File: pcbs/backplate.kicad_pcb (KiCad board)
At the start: 2 copper layers, 130.3 x 107.9 mm, 5 parts

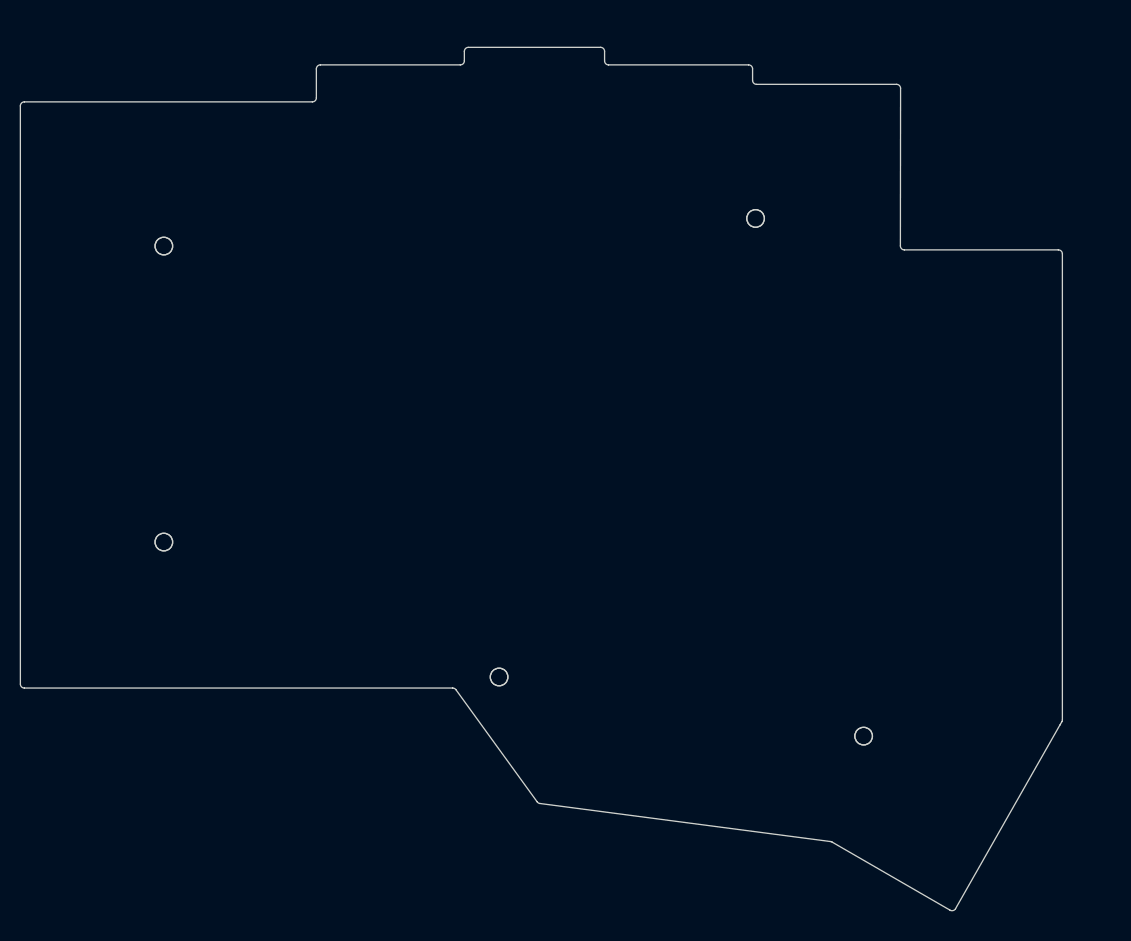
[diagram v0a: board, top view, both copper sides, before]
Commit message: fix(pcb): increase key spacing and correct power switch
Set the PG1316S key pitch to 19.5 mm in both axes and regenerate the tracked PCB and outline artifacts.

Keep the power switch mapping consistent with the intended on/off orientation while preserving the original board outline.
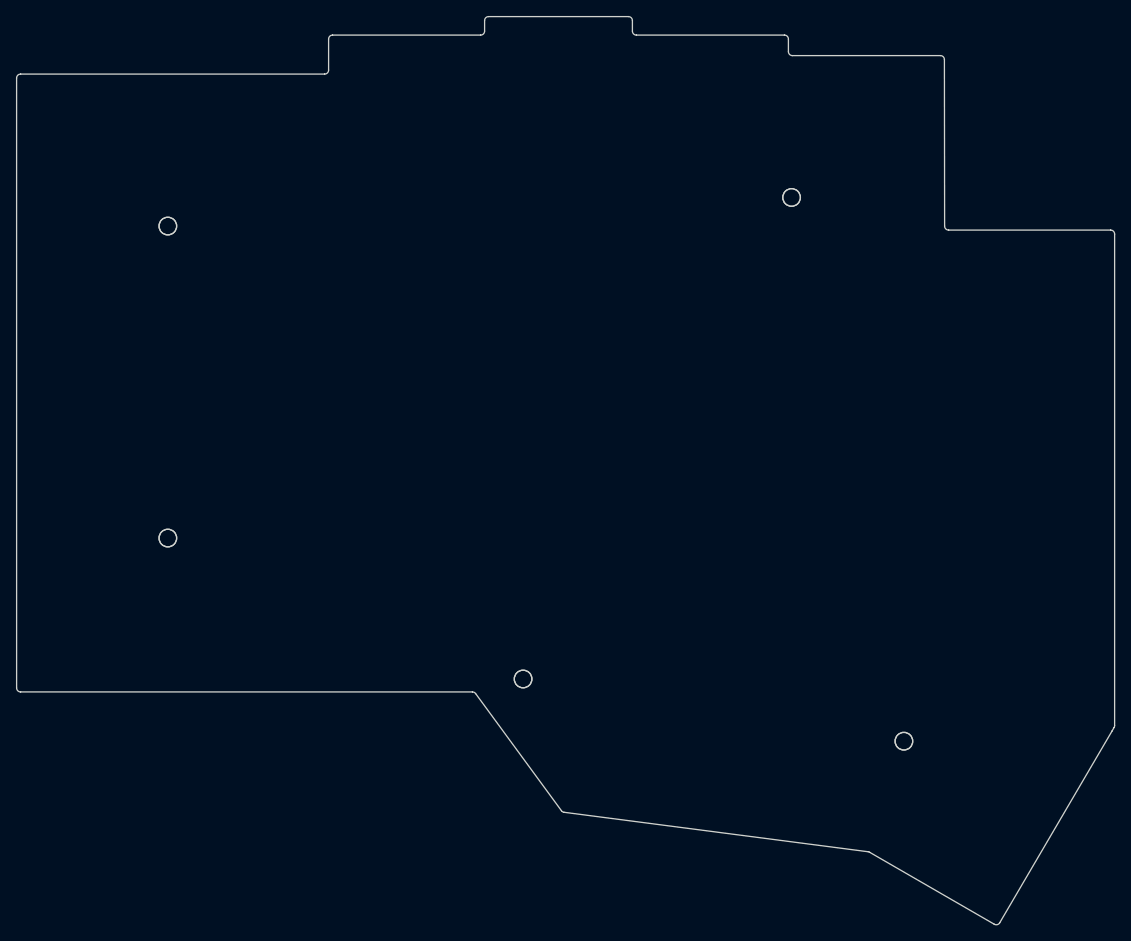
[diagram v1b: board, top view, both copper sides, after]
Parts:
- moved MH3 5.21 mm to (187.7, 47.7)
- moved MH5 5.07 mm to (201.8, 115.6)
- moved MH4 3.01 mm to (154.2, 107.9)
- moved MH1 2.55 mm to (109.8, 51.2)
- moved MH2 0.71 mm to (109.8, 90.2)
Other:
- board size 130.3 x 107.9 mm -> 137.3 x 113.5 mm

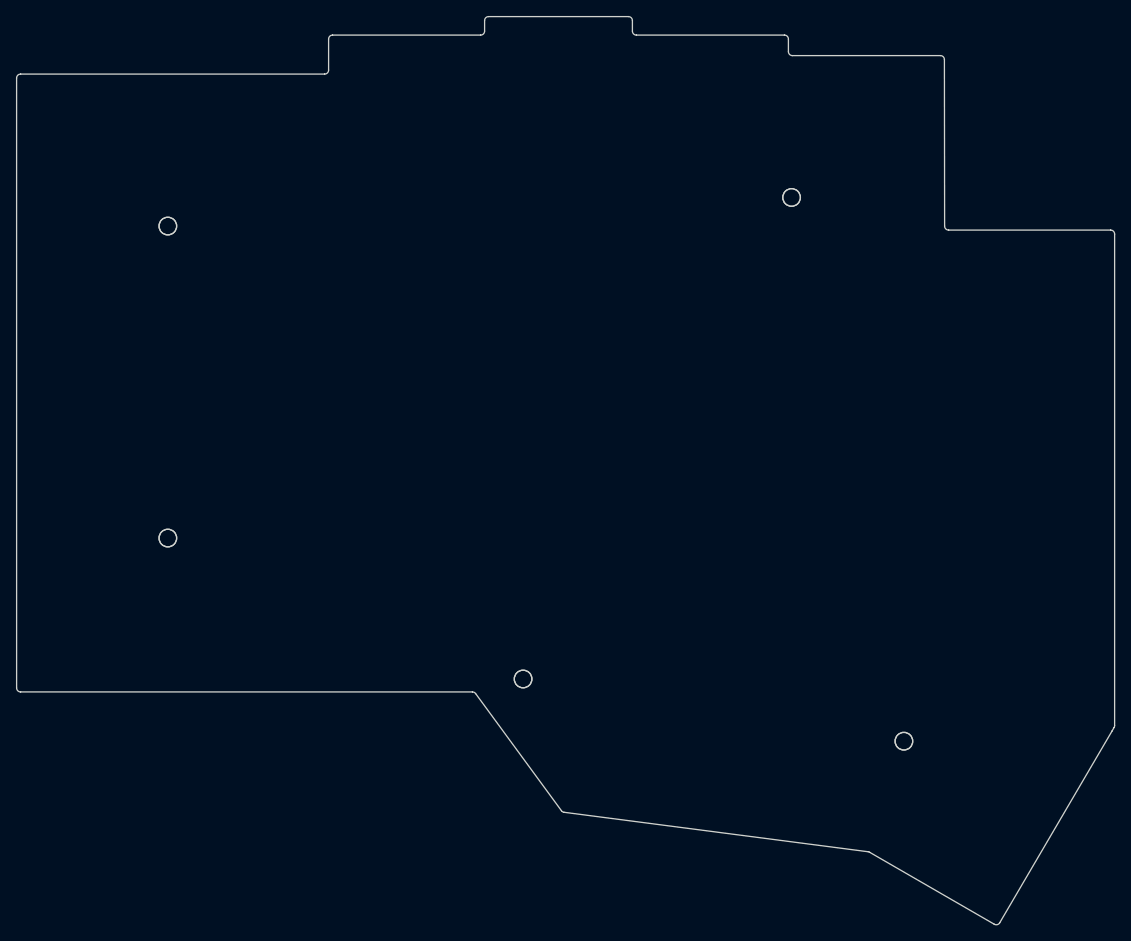
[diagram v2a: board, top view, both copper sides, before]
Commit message: feat: default to compact 18.5 mm layout and refresh generated boards
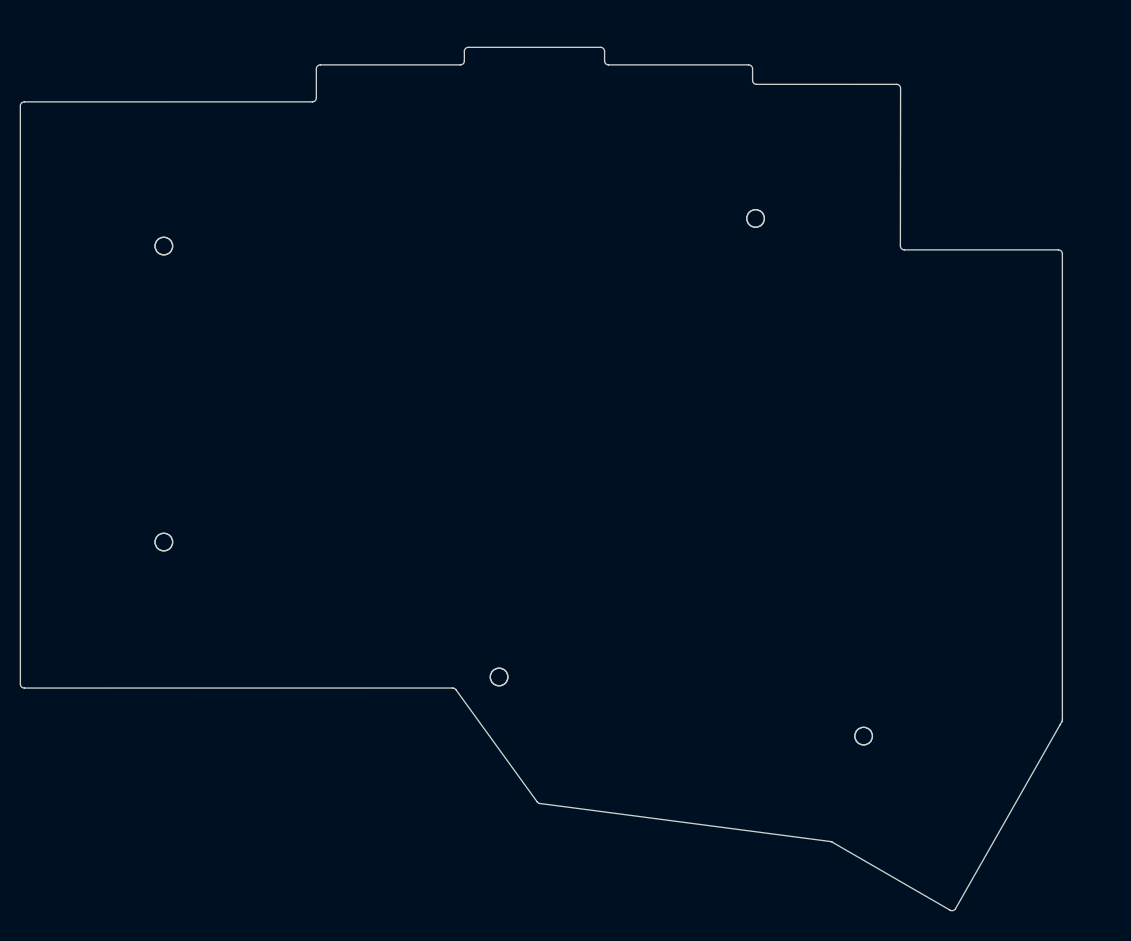
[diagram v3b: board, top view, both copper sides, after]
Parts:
- moved MH3 5.21 mm to (183.2, 50.3)
- moved MH5 5.07 mm to (196.7, 115.0)
- moved MH4 3.01 mm to (151.2, 107.6)
- moved MH1 2.55 mm to (109.2, 53.8)
- moved MH2 0.71 mm to (109.2, 90.8)
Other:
- board size 137.3 x 113.5 mm -> 130.3 x 107.9 mm
